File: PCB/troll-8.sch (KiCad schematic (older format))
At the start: 28 parts, among them P101 SPI_EXT, P104 Audio Out, P105 AOUT, U101 4050, U102 74LVC138, U103 arduino_nano

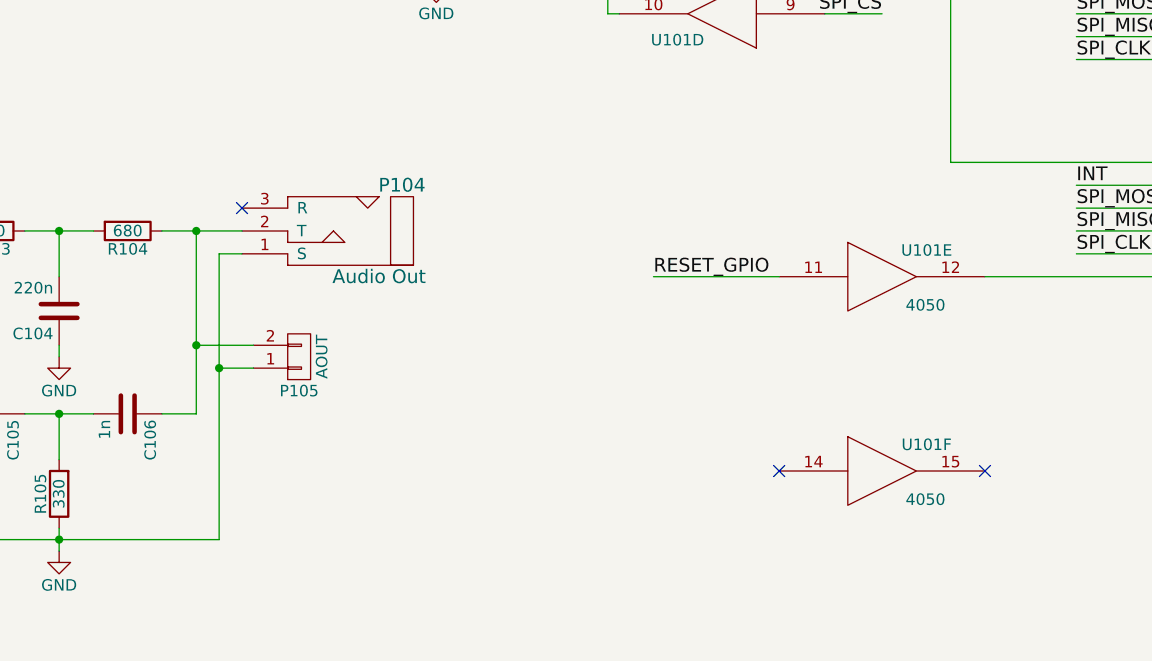
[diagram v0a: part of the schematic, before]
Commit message: redesign, logo and audio connector changed
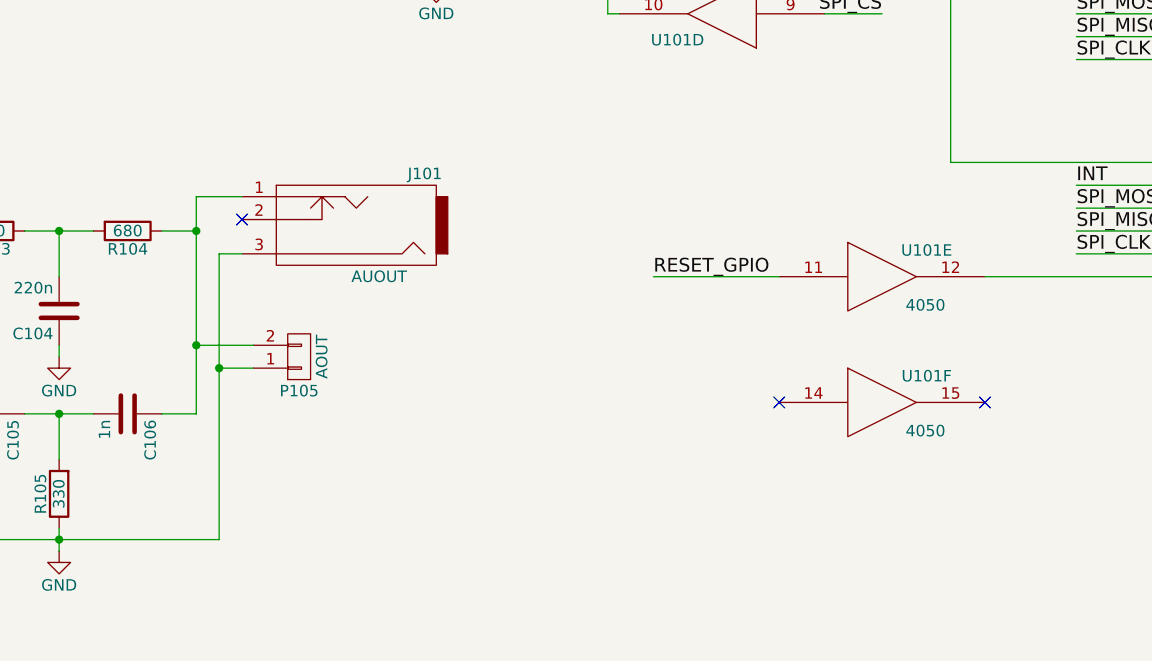
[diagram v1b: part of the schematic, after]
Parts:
- removed P104: Audio Out, modules:LUM150302, symbol TRS-3
- added J101: AUOUT, connectors:THONKICONN, symbol JACK_2P
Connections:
- net GND: now also J101.3
- net at C106.1, P105.2 (P2), R104.1: now also J101.1
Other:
- moved on the sheet: U101F
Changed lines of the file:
@@
 	1    0    0    -1
-$EndComp
-$Comp
-L TRS-3 P104
-U 1 1 5682F819
-P 6000 5000
-F 0 "P104" H 6100 5000 60  0000 C CNN
-F 1 "Audio Out" H 6200 4600 60  0000 C CNN
-F 2 "modules:LUM150302" H 6000 5000 60  0001 C CNN
-F 3 "" H 6000 5000 60  0000 C CNN
-	1    6000 5000
-	-1   0    0    -1
 $EndComp
 Text Label 2800 5200 0    60   ~ 0
@@
 	1    0    0    -1
 $EndComp
-NoConn ~ 5200 5100
 NoConn ~ 4100 1000
 $Comp
@@
 L 4050 U101
 U 6 1 56878395
-P 8000 6250
-F 0 "U101" H 8195 6365 50  0000 C CNN
-F 1 "4050" H 8190 6125 50  0000 C CNN
-F 2 "Housings_SSOP:TSSOP-16_4.4x5mm_Pitch0.65mm" H 8000 6250 60  0001 C CNN
-F 3 "" H 8000 6250 60  0000 C CNN
-	6    8000 6250
-	1    0    0    -1
-$EndComp
-NoConn ~ 8450 6250
-NoConn ~ 7550 6250
+P 8000 5950
+F 0 "U101" H 8195 6065 50  0000 C CNN
+F 1 "4050" H 8190 5825 50  0000 C CNN
+F 2 "Housings_SSOP:TSSOP-16_4.4x5mm_Pitch0.65mm" H 8000 5950 60  0001 C CNN
+F 3 "" H 8000 5950 60  0000 C CNN
+	6    8000 5950
+	1    0    0    -1
+$EndComp
+NoConn ~ 8450 5950
+NoConn ~ 7550 5950
 $Comp
 L R R101
@@
 Connection ~ 4400 6000
 Wire Wire Line
-	4850 5200 5200 5200
-Wire Wire Line
-	5000 5200 5000 6000
+	5000 5050 5000 6000
 Wire Wire Line
 	5000 6000 4850 6000
@@
 	3600 1000 3600 800
 NoConn ~ 4150 3750
+$Comp
+L JACK_2P J101
+U 1 1 5A1D7B76
+P 5650 5150
+F 0 "J101" H 5300 4950 50  0000 C CNN
+F 1 "AUOUT" H 5500 5400 50  0000 C CNN
+F 2 "connectors:THONKICONN" H 5650 5150 50  0001 C CNN
+F 3 "" H 5650 5150 50  0000 C CNN
+	1    5650 5150
+	-1   0    0    1
+$EndComp
+Wire Wire Line
+	4850 5200 5000 5200
+Wire Wire Line
+	5200 5050 5000 5050
+NoConn ~ 5200 5150
 $EndSCHEMATC
